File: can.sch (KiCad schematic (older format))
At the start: 13 parts, among them P8 CAN, U10 MCP2551-I/SN, U11 MCP2515, U12 SG-210STF_16MHz

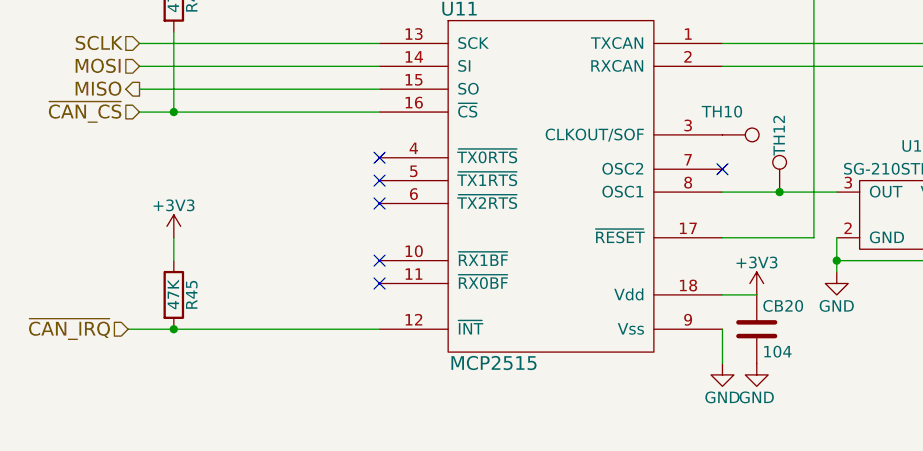
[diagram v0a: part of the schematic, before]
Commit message: Deleted unnecessary files and splitting schmatics.
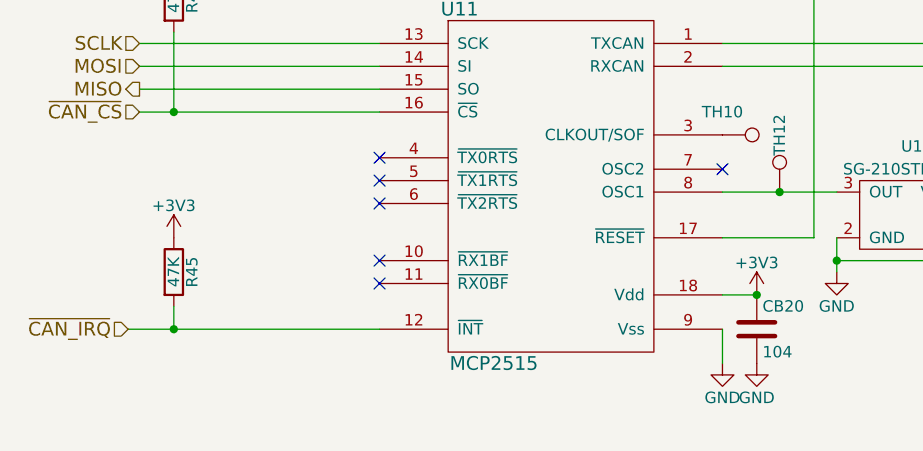
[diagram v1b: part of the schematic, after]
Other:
- moved on the sheet: R45
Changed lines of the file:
@@
 $Descr A4 11693 8268
 encoding utf-8
-Sheet 4 6
-Title ""
+Sheet 4 8
+Title "DCoJA Yatagarasu Mezzanine"
 Date ""
 Rev ""
-Comp ""
-Comment1 ""
-Comment2 ""
-Comment3 ""
-Comment4 ""
+Comp "DroneWorks Inc."
+Comment1 "Copyright (c) 2016 DroneWorks Inc."
+Comment2 "All rights reserved."
+Comment3 "Creative Commons  (CC BY-SA 4.0)"
+Comment4 "Designed by: Michihiro Imaoka (@imaoca)"
 $EndDescr
 $Comp
@@
 SCLK
 $Comp
-L GND #PWR083
+L GND #PWR071
 U 1 1 56F7CBF7
 P 5350 4600
-F 0 "#PWR083" H 5350 4350 50  0001 C CNN
+F 0 "#PWR071" H 5350 4350 50  0001 C CNN
 F 1 "GND" H 5350 4450 50  0000 C CNN
 F 2 "" H 5350 4600 50  0000 C CNN
@@
 $EndComp
 $Comp
-L GND #PWR084
+L GND #PWR072
 U 1 1 56F7CC0F
 P 7200 4700
-F 0 "#PWR084" H 7200 4450 50  0001 C CNN
+F 0 "#PWR072" H 7200 4450 50  0001 C CNN
 F 1 "GND" H 7200 4550 50  0000 C CNN
 F 2 "" H 7200 4700 50  0000 C CNN
@@
 $EndComp
 $Comp
-L GND #PWR085
+L GND #PWR073
 U 1 1 56F7CC24
 P 7750 4700
-F 0 "#PWR085" H 7750 4450 50  0001 C CNN
+F 0 "#PWR073" H 7750 4450 50  0001 C CNN
 F 1 "GND" H 7750 4550 50  0000 C CNN
 F 2 "" H 7750 4700 50  0000 C CNN
@@
 $EndComp
 $Comp
-L +5V #PWR086
+L +5V #PWR074
 U 1 1 56F7CC75
 P 7750 2450
-F 0 "#PWR086" H 7750 2300 50  0001 C CNN
+F 0 "#PWR074" H 7750 2300 50  0001 C CNN
 F 1 "+5V" H 7750 2590 50  0000 C CNN
 F 2 "" H 7750 2450 50  0000 C CNN
@@
 L R R45
 U 1 1 570269E4
-P 2950 4300
-F 0 "R45" V 3030 4300 50  0000 C CNN
-F 1 "47K" V 2950 4300 50  0000 C CNN
-F 2 "Resistors_SMD:R_0603_HandSoldering" V 2880 4300 50  0001 C CNN
-F 3 "" H 2950 4300 50  0000 C CNN
-	1    2950 4300
+P 2950 4200
+F 0 "R45" V 3030 4200 50  0000 C CNN
+F 1 "47K" V 2950 4200 50  0000 C CNN
+F 2 "Resistors_SMD:R_0603_HandSoldering" V 2880 4200 50  0001 C CNN
+F 3 "" H 2950 4200 50  0000 C CNN
+	1    2950 4200
 	1    0    0    -1
 $EndComp
@@
 	8250 3600 8250 3650
 Connection ~ 8550 3650
-Wire Wire Line
-	2950 4150 2950 4050
 Connection ~ 2950 4450
 Wire Wire Line
@@
 NoConn ~ 5350 3750
 $Comp
-L GND #PWR087
+L GND #PWR075
 U 1 1 56FF16F6
 P 5850 4200
-F 0 "#PWR087" H 5850 3950 50  0001 C CNN
+F 0 "#PWR075" H 5850 3950 50  0001 C CNN
 F 1 "GND" H 5850 4050 50  0000 C CNN
 F 2 "" H 5850 4200 50  0000 C CNN
@@
 $EndComp
 $Comp
-L GND #PWR088
+L GND #PWR076
 U 1 1 5707F07C
 P 7950 2850
-F 0 "#PWR088" H 7950 2600 50  0001 C CNN
+F 0 "#PWR076" H 7950 2600 50  0001 C CNN
 F 1 "GND" H 7950 2700 50  0000 C CNN
 F 2 "" H 7950 2850 50  0000 C CNN
@@
 $EndComp
 $Comp
-L GND #PWR089
+L GND #PWR077
 U 1 1 5707F128
 P 5500 4600
-F 0 "#PWR089" H 5500 4350 50  0001 C CNN
+F 0 "#PWR077" H 5500 4350 50  0001 C CNN
 F 1 "GND" H 5500 4450 50  0000 C CNN
 F 2 "" H 5500 4600 50  0000 C CNN
@@
 Connection ~ 2950 3500
 $Comp
-L +3V3 #PWR090
+L +3V3 #PWR078
 U 1 1 570745B9
 P 2950 2850
-F 0 "#PWR090" H 2950 2700 50  0001 C CNN
+F 0 "#PWR078" H 2950 2700 50  0001 C CNN
 F 1 "+3V3" H 2950 2990 50  0000 C CNN
 F 2 "" H 2950 2850 50  0000 C CNN
@@
 $EndComp
 $Comp
-L +3V3 #PWR091
+L +3V3 #PWR079
 U 1 1 570745E9
 P 2950 4050
-F 0 "#PWR091" H 2950 3900 50  0001 C CNN
+F 0 "#PWR079" H 2950 3900 50  0001 C CNN
 F 1 "+3V3" H 2950 4190 50  0000 C CNN
 F 2 "" H 2950 4050 50  0000 C CNN
@@
 $EndComp
 $Comp
-L +3V3 #PWR092
+L +3V3 #PWR080
 U 1 1 5707487A
 P 5500 4300
-F 0 "#PWR092" H 5500 4150 50  0001 C CNN
+F 0 "#PWR080" H 5500 4150 50  0001 C CNN
 F 1 "+3V3" H 5500 4440 50  0000 C CNN
 F 2 "" H 5500 4300 50  0000 C CNN
@@
 $EndComp
 $Comp
-L +3V3 #PWR093
+L +3V3 #PWR081
 U 1 1 570748DE
 P 6650 3850
-F 0 "#PWR093" H 6650 3700 50  0001 C CNN
+F 0 "#PWR081" H 6650 3700 50  0001 C CNN
 F 1 "+3V3" H 6650 3990 50  0000 C CNN
 F 2 "" H 6650 3850 50  0000 C CNN
@@
 NoConn ~ 8900 3350
 NoConn ~ 8900 3650
+Connection ~ 5500 4300
+Wire Wire Line
+	2950 4350 2950 4450
 $EndSCHEMATC
